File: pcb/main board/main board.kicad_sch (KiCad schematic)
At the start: 8 parts, among them J1 Motor Conn 0, J2 Motor Conn 1, J3 Motor Conn 2, J4 Motor Conn 3, U1 L298HN, U2 L298HN

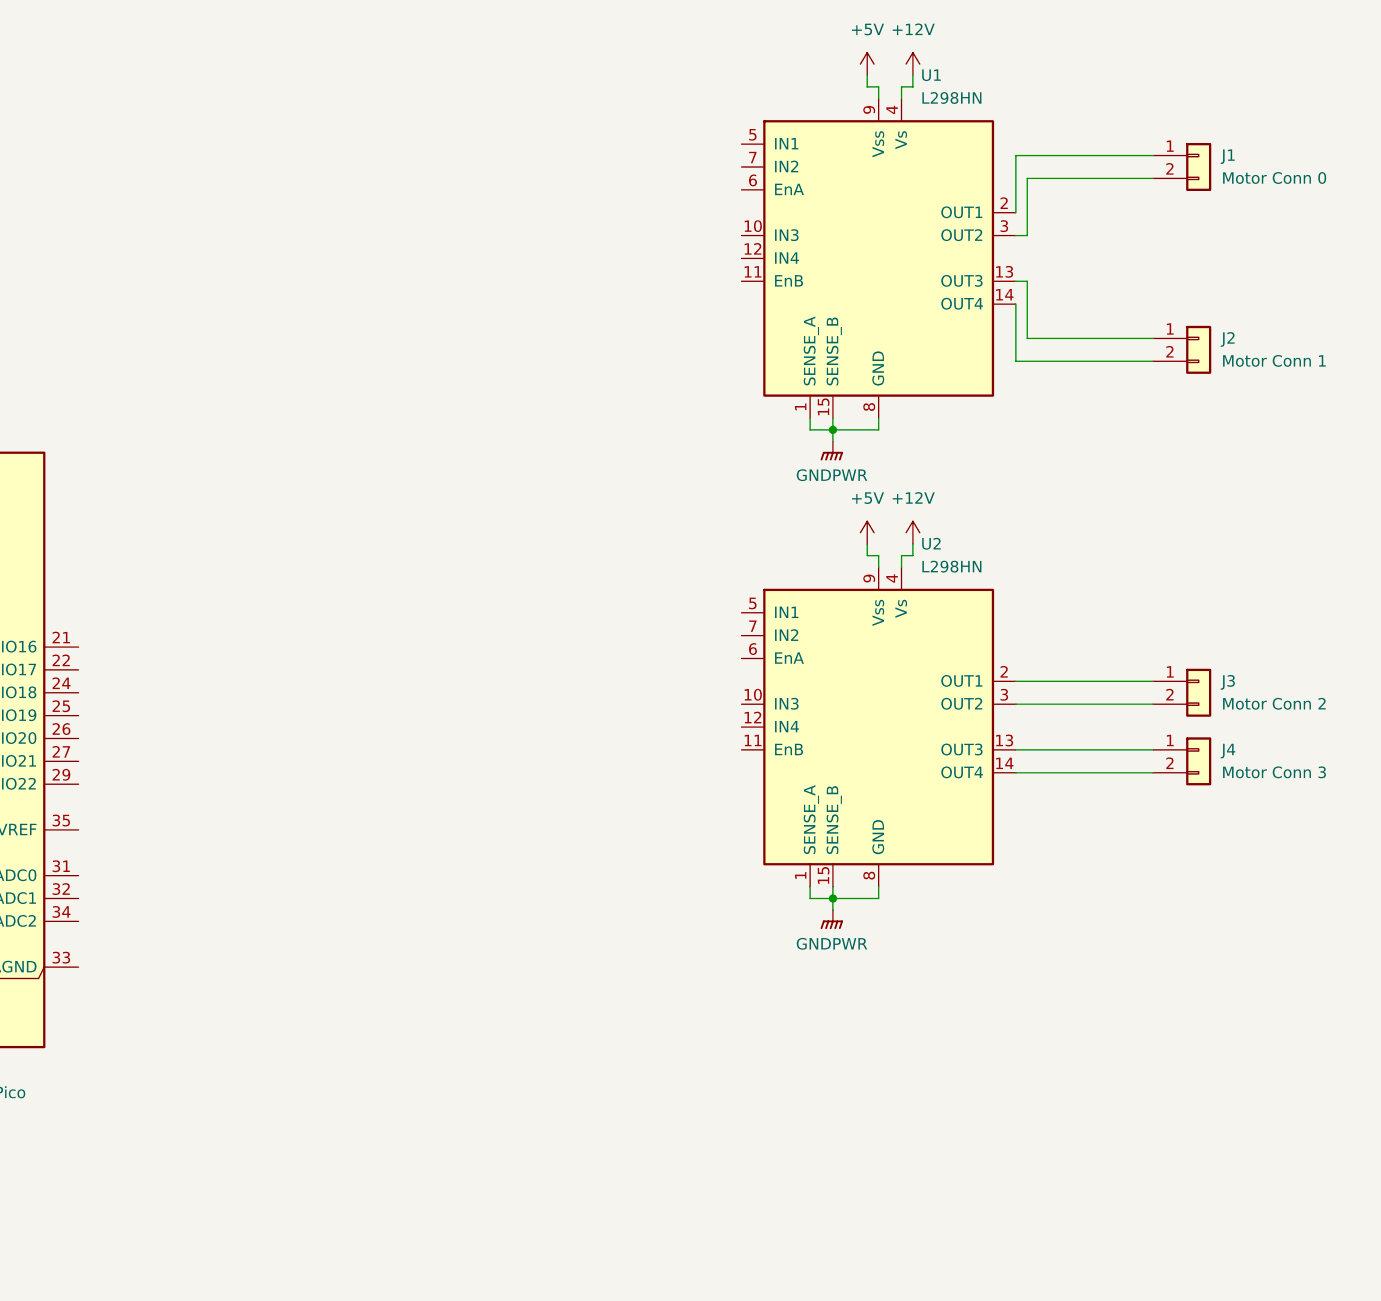
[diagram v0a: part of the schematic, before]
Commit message: Finished motor driver on main pcb
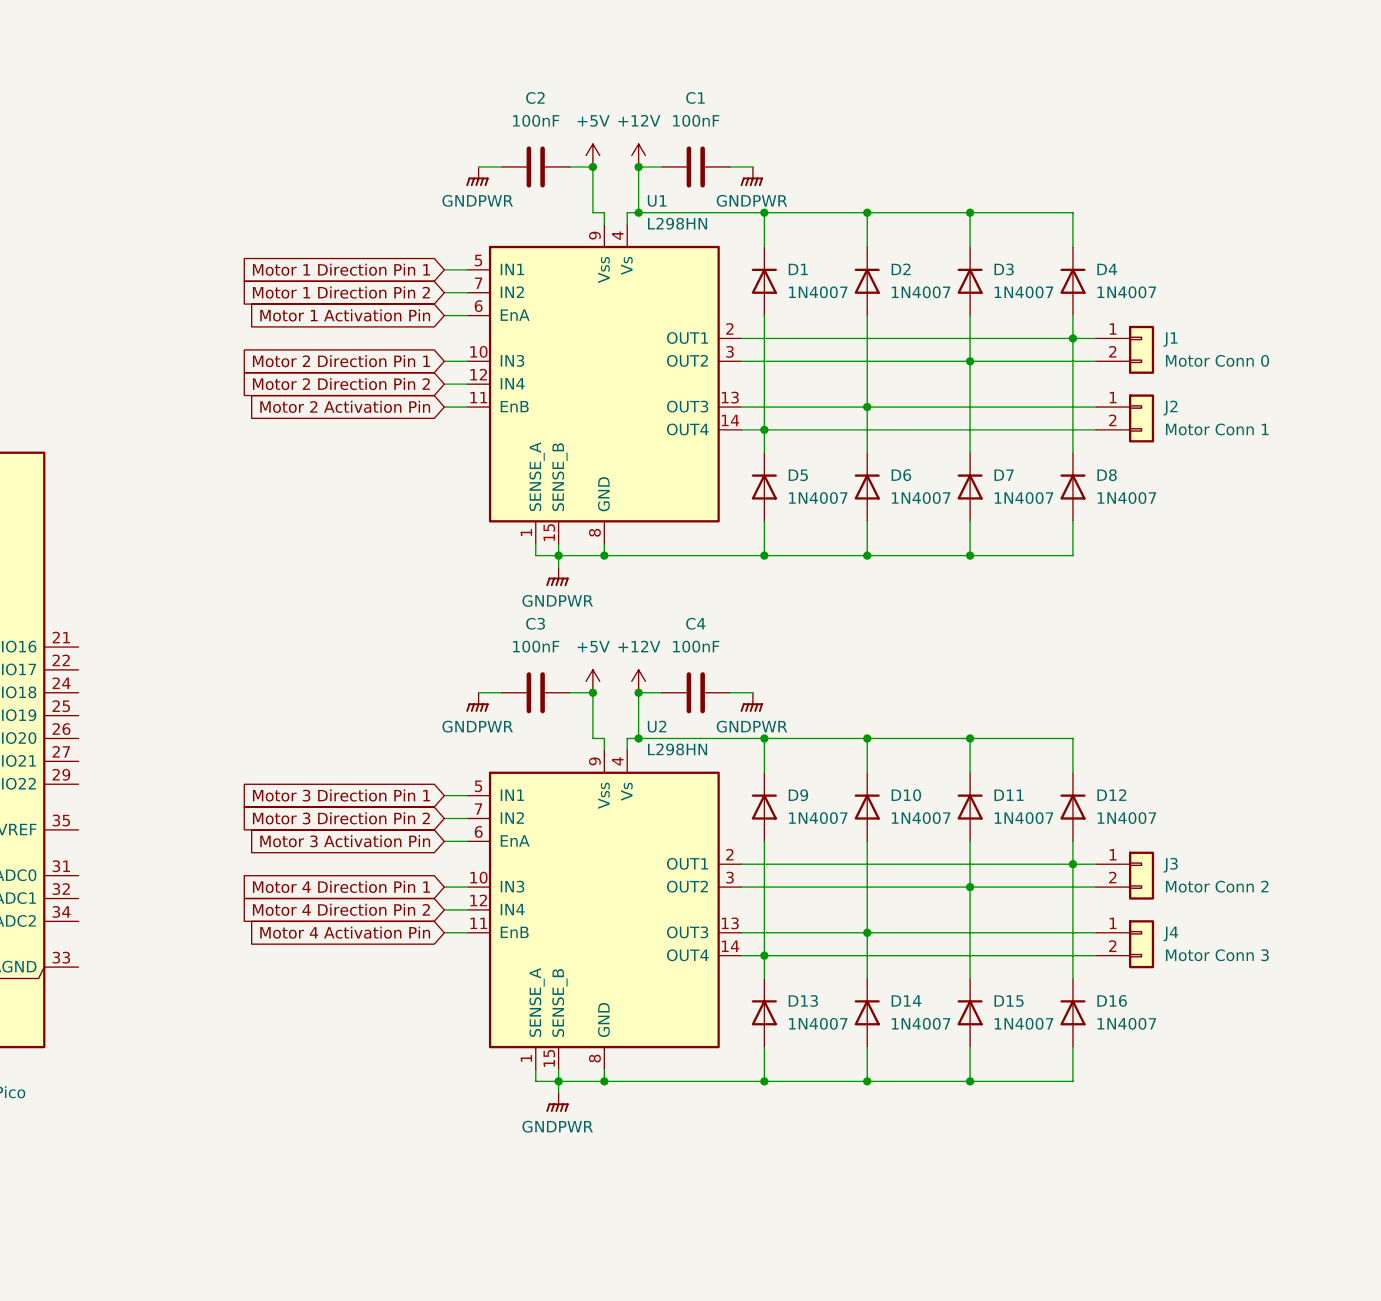
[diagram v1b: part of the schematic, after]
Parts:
- added C1, C2, C3, C4: 100nF, symbol Device:C
- added D1, D10, D11, D12, D13, D14, D15, D16, D2, D3, D4, D5, D6, D7, D8, D9: 1N4007, Diode_THT:D_DO-41_SOD81_P10.16mm_Horizontal, symbol Diode:1N4007
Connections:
- net +12V: now also C1.1, C4.1, D1.1 (K), D10.1 (K), D11.1 (K), D12.1 (K), D2.1 (K), D3.1 (K), D4.1 (K), D9.1 (K)
- net +5V: now also C2.2, C3.2
- net GNDPWR: now also C1.2, C2.1, C3.1, C4.2, D13.2 (A), D14.2 (A), D15.2 (A), D16.2 (A), D5.2 (A), D6.2 (A), D7.2 (A), D8.2 (A)
- net at J1.1 (Pin_1), U1.2 (OUT1): now also D4.2 (A), D8.1 (K)
- net at J1.2 (Pin_2), U1.3 (OUT2): now also D3.2 (A), D7.1 (K)
- net Motor 2 Direction Pin 1: now reaches U1.10 (IN3)
- net Motor 2 Activation Pin: now reaches U1.11 (EnB)
- net Motor 2 Direction Pin 2: now reaches U1.12 (IN4)
- net at J2.1 (Pin_1), U1.13 (OUT3): now also D2.2 (A), D6.1 (K)
- net at J2.2 (Pin_2), U1.14 (OUT4): now also D1.2 (A), D5.1 (K)
- net Motor 1 Direction Pin 1: now reaches U1.5 (IN1)
- net Motor 1 Activation Pin: now reaches U1.6 (EnA)
- net Motor 1 Direction Pin 2: now reaches U1.7 (IN2)
- net at J3.1 (Pin_1), U2.2 (OUT1): now also D12.2 (A), D16.1 (K)
- net at J3.2 (Pin_2), U2.3 (OUT2): now also D11.2 (A), D15.1 (K)
- net Motor 4 Direction Pin 1: now reaches U2.10 (IN3)
- net Motor 4 Activation Pin: now reaches U2.11 (EnB)
- net Motor 4 Direction Pin 2: now reaches U2.12 (IN4)
- net at J4.1 (Pin_1), U2.13 (OUT3): now also D10.2 (A), D14.1 (K)
- net at J4.2 (Pin_2), U2.14 (OUT4): now also D13.1 (K), D9.2 (A)
- net Motor 3 Direction Pin 1: now reaches U2.5 (IN1)
- net Motor 3 Activation Pin: now reaches U2.6 (EnA)
- net Motor 3 Direction Pin 2: now reaches U2.7 (IN2)
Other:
- moved on the sheet: J1, J2, J3, J4, U1, U2

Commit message: Added logical 5v regulator schematic
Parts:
- added C5: 680uF, symbol Device:C_Polarized
- added C6: 220uF, symbol Device:C_Polarized
- added D17: 1N5824, Diode_THT:D_DO-201AD_P15.24mm_Horizontal, symbol Diode:1N5822
- added L1: 33uH, symbol Device:L
- added U3: LM2596S-5, Package_TO_SOT_SMD:TO-263-5_TabPin3, symbol Regulator_Switching:LM2596S-5
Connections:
- net +12V: now also C2.2, C5.1, U3.1 (VIN); no longer C1.1
- net GNDPWR: now also A1.13 (GND), A1.18 (GND), A1.23 (GND), A1.28 (GND), A1.3 (GND), A1.38 (GND), A1.8 (GND), C5.2, C6.2, D17.2 (A), U3.3 (GND), U3.5 (~{ON}/OFF)
- net Motor 1 Activation Pin: now also A1.1 (GPIO0)
- net Motor 1 Direction Pin 1: now also A1.6 (GPIO4)
- net Motor 1 Direction Pin 2: now also A1.7 (GPIO5)
- net Motor 2 Activation Pin: now also A1.2 (GPIO1)
- net Motor 2 Direction Pin 1: now also A1.9 (GPIO6)
- net Motor 2 Direction Pin 2: now also A1.10 (GPIO7)
- net Motor 3 Activation Pin: now also A1.4 (GPIO2)
- net Motor 3 Direction Pin 1: now also A1.11 (GPIO8)
- net Motor 3 Direction Pin 2: now also A1.12 (GPIO9)
- net Motor 4 Activation Pin: now also A1.5 (GPIO3)
- net Motor 4 Direction Pin 1: now also A1.14 (GPIO10)
- net Motor 4 Direction Pin 2: now also A1.15 (GPIO11)
- net I2C 0 SDA: now reaches A1.21 (GPIO16)
- net I2C 0 SCL: now reaches A1.22 (GPIO17)
- net +5VL: now reaches A1.40 (VBUS)
- net +5VL: now also C1.1, C3.2, U1.9 (Vss), U2.9 (Vss), C6.1, L1.2, U3.4 (FB)
- removed net +5V: C2.2, C3.2, U1.9 (Vss), U2.9 (Vss)
- new net: D17.1 (K), L1.1, U3.2 (OUT)
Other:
- moved on the sheet: A1, A2, C1, C2, C3, C4, D1, D10, D11, D12, D13, D14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

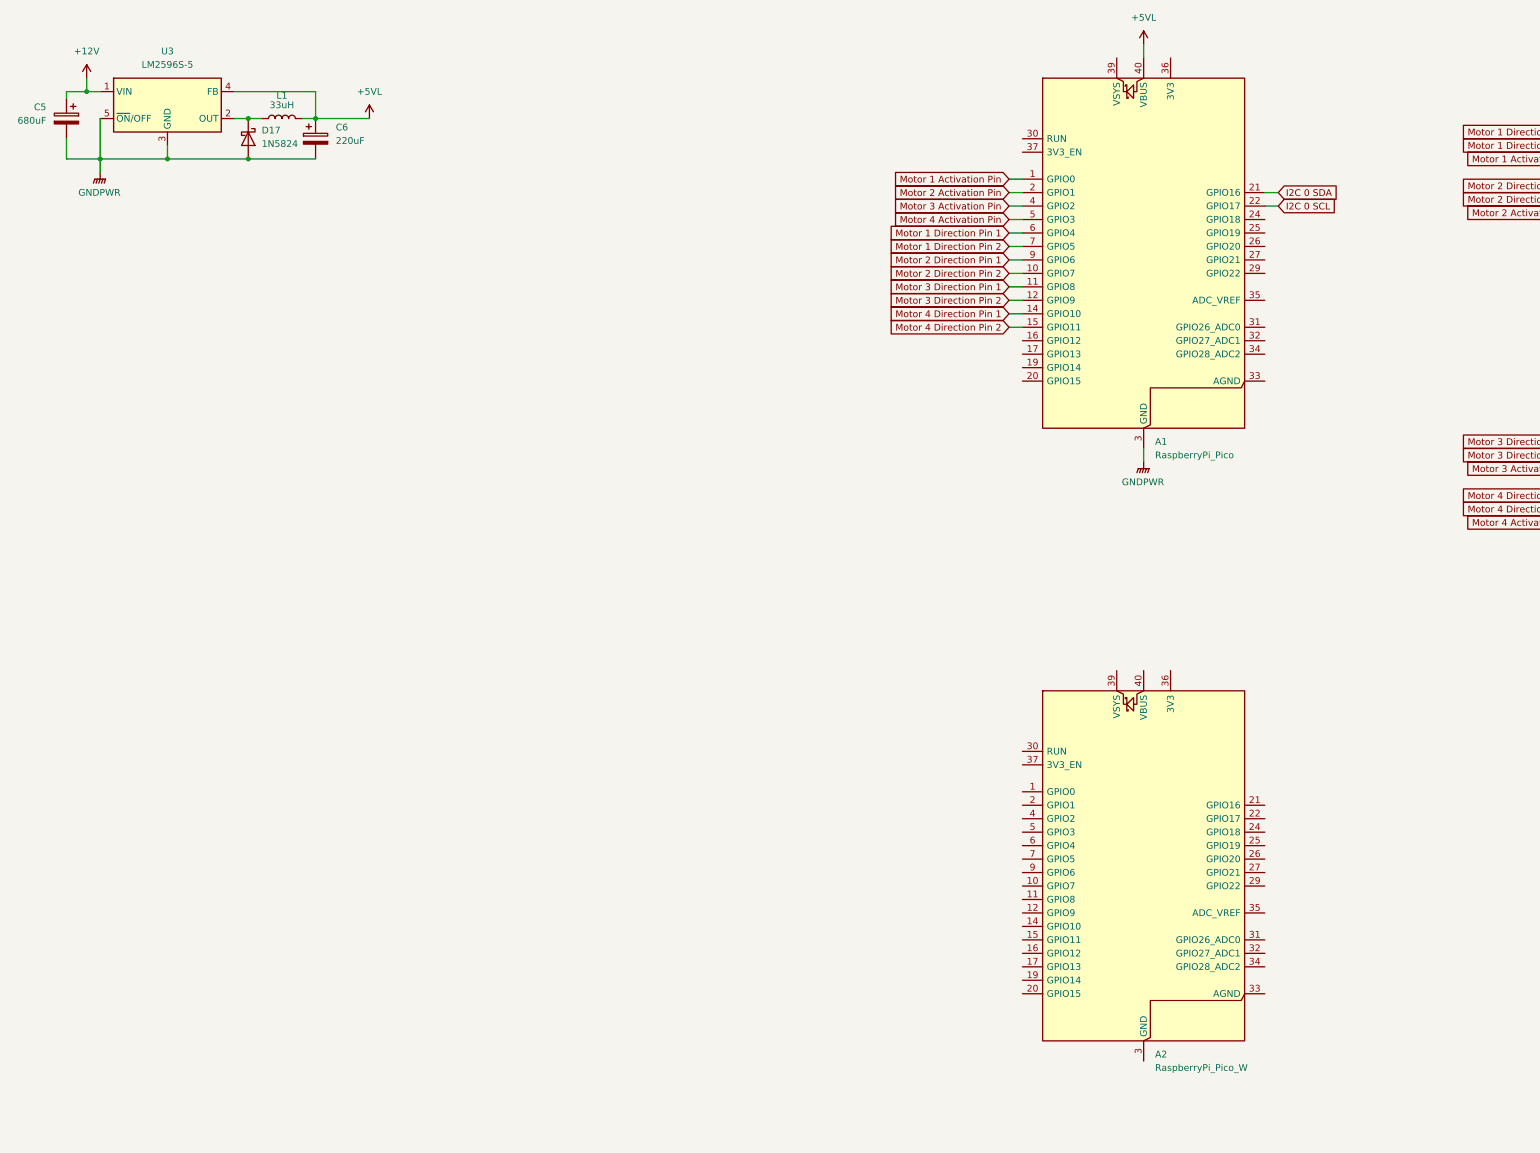
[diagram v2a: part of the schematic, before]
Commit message: Added MCP23017 gpio extender to the motor driver and found a 8A 5v regulator. Neither of them are connected correctly
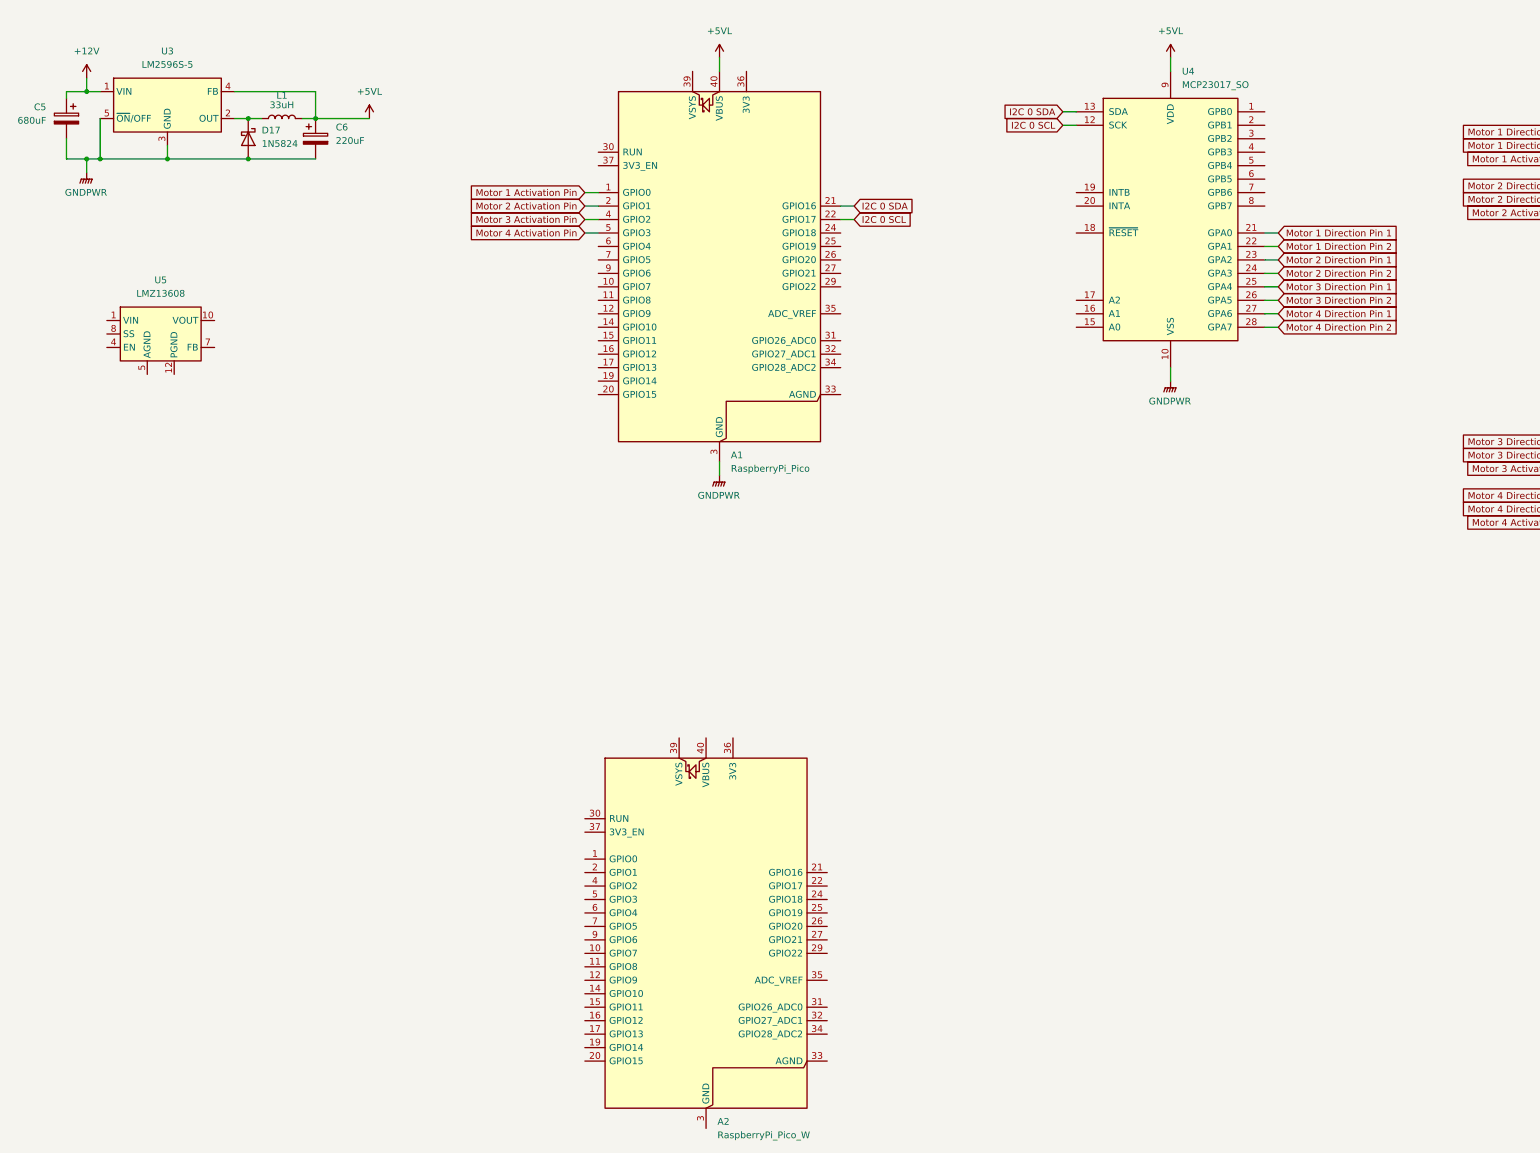
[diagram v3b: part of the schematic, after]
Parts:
- added U4: MCP23017_SO, Package_SO:SOIC-28W_7.5x17.9mm_P1.27mm, symbol Interface_Expansion:MCP23017_SO
- added U5: LMZ13608, Package_TO_SOT_SMD:Texas_NDY0011A, symbol Regulator_Switching:LMZ13608
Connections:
- net +5VL: now also U4.9 (VDD)
- net GNDPWR: now also U4.10 (VSS)
- net I2C 0 SCL: now also U4.12 (SCK)
- net I2C 0 SDA: now also U4.13 (SDA)
- net Motor 1 Direction Pin 1: now also U4.21 (GPA0); no longer A1.6 (GPIO4)
- net Motor 1 Direction Pin 2: now also U4.22 (GPA1); no longer A1.7 (GPIO5)
- net Motor 2 Direction Pin 1: now also U4.23 (GPA2); no longer A1.9 (GPIO6)
- net Motor 2 Direction Pin 2: now also U4.24 (GPA3); no longer A1.10 (GPIO7)
- net Motor 3 Direction Pin 1: now also U4.25 (GPA4); no longer A1.11 (GPIO8)
- net Motor 3 Direction Pin 2: now also U4.26 (GPA5); no longer A1.12 (GPIO9)
- net Motor 4 Direction Pin 1: now also U4.27 (GPA6); no longer A1.14 (GPIO10)
- net Motor 4 Direction Pin 2: now also U4.28 (GPA7); no longer A1.15 (GPIO11)
- new net: U5.1 (VIN), U5.2 (VIN)
- new net: U5.10 (VOUT), U5.11 (VOUT)
- new net: U5.3 (AGND), U5.5 (AGND), U5.6 (AGND)
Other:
- moved on the sheet: A1, A2
